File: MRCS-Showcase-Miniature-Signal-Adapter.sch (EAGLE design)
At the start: 18 parts

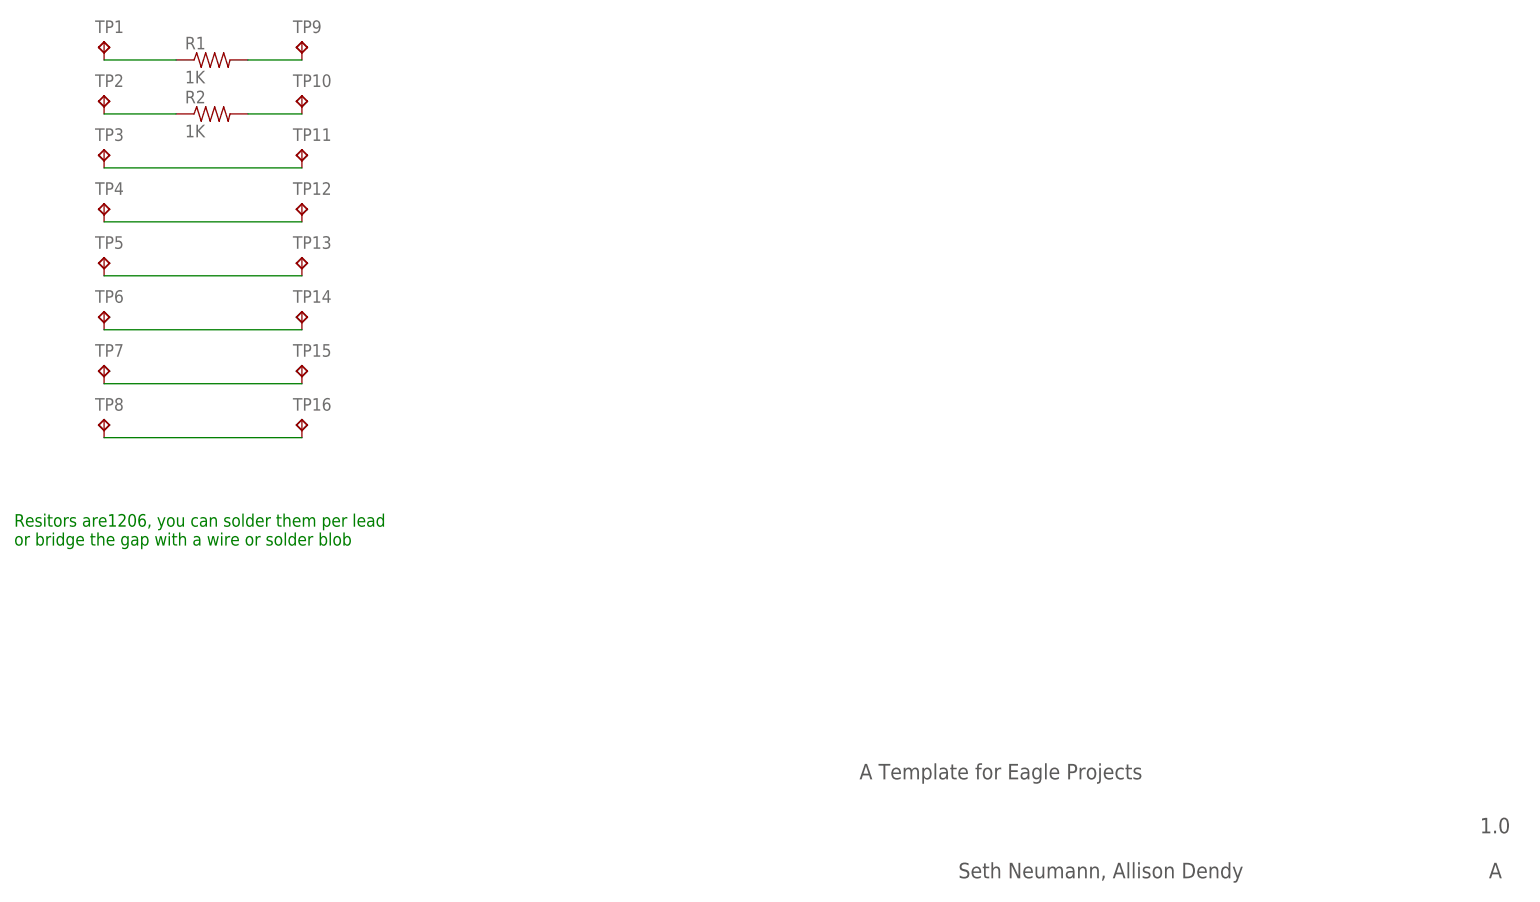
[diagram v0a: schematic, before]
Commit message: First production version
Showcase miniature signal base for 1 or 2 head signal, requested by Allison Dendy
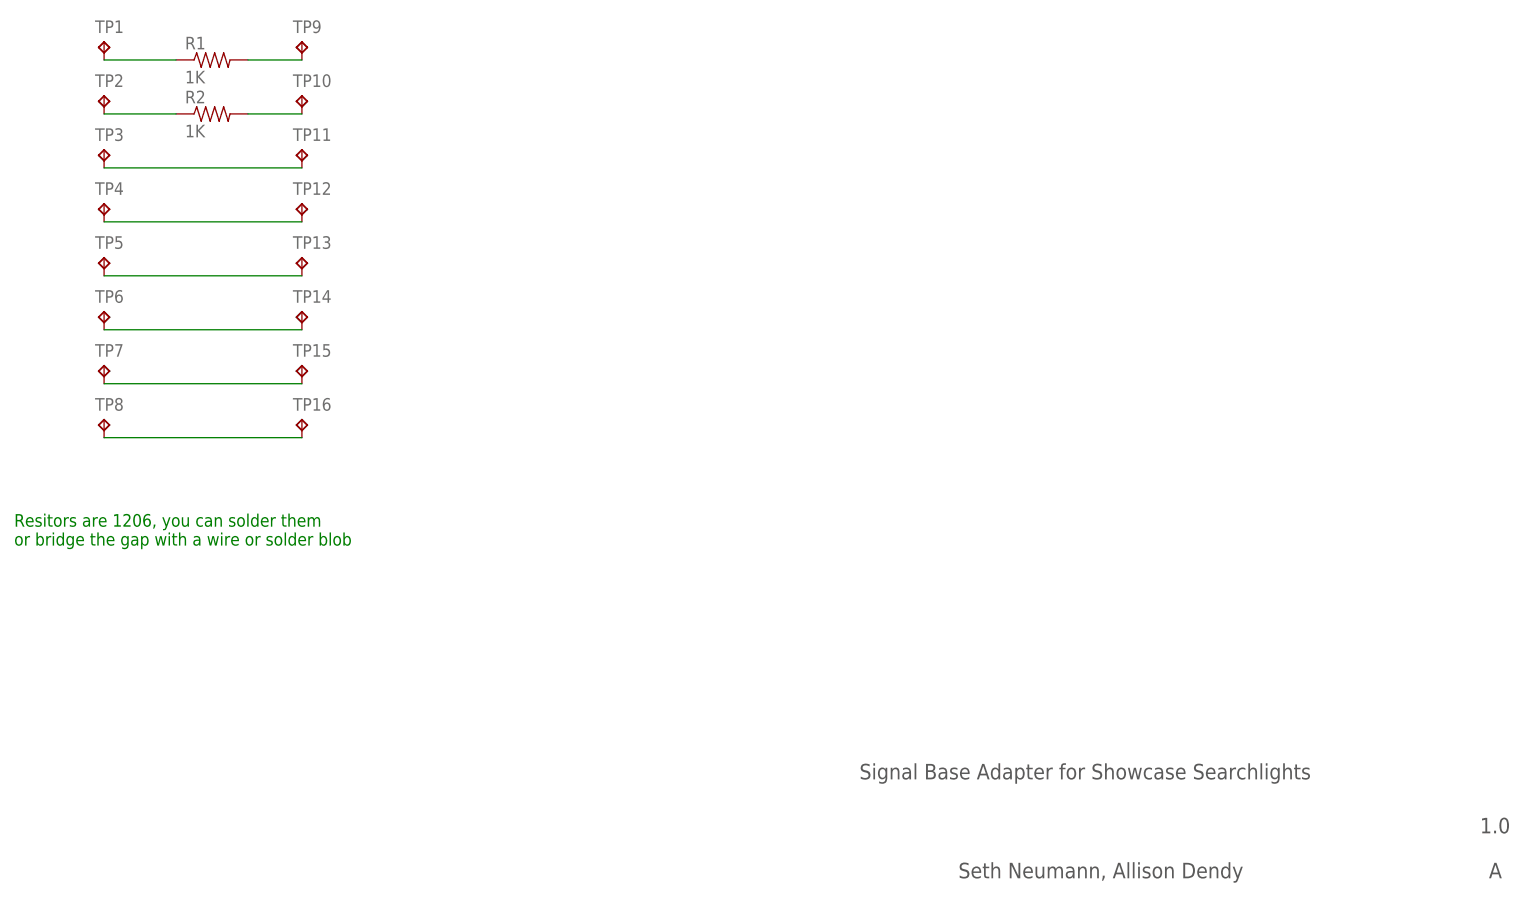
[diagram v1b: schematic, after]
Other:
- note added: "Resitors are 1206, you can solder them or bridge the gap with a wire or solder blob"
- note added: "Signal Base Adapter for Showcase Searchlights"
- note removed: "A Template for Eagle Projects"
- note removed: "Resitors are1206, you can solder them per lead or bridge the gap with a wire or solder blob"
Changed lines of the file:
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@@
 <sheet>
 <plain>
-<text x="152.4" y="20.32" size="2.1844" layer="97">A Template for Eagle Projects</text>
+<text x="152.4" y="20.32" size="2.1844" layer="97">Signal Base Adapter for Showcase Searchlights</text>
 <text x="240.03" y="12.7" size="2.1844" layer="97">1.0</text>
 <text x="241.3" y="6.35" size="2.1844" layer="97">A</text>
 <text x="166.37" y="6.35" size="2.1844" layer="97">Seth Neumann, Allison Dendy</text>
-<text x="33.02" y="53.34" size="1.778" layer="91">Resitors are1206, you can solder them per lead
+<text x="33.02" y="53.34" size="1.778" layer="91">Resitors are 1206, you can solder them
 or bridge the gap with a wire or solder blob</text>
 </plain>
